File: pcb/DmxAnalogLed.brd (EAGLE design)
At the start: 69 parts, among them IC2 7805TV, J1 RS485, J2 POWER_JACKPTH, J3 RS485, Q1 16MHz 10ppm, U1 ARDUINO_LEONARDO-REV3B_SMARTP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, U2 SN75176ASOIC, X1 USBPTH

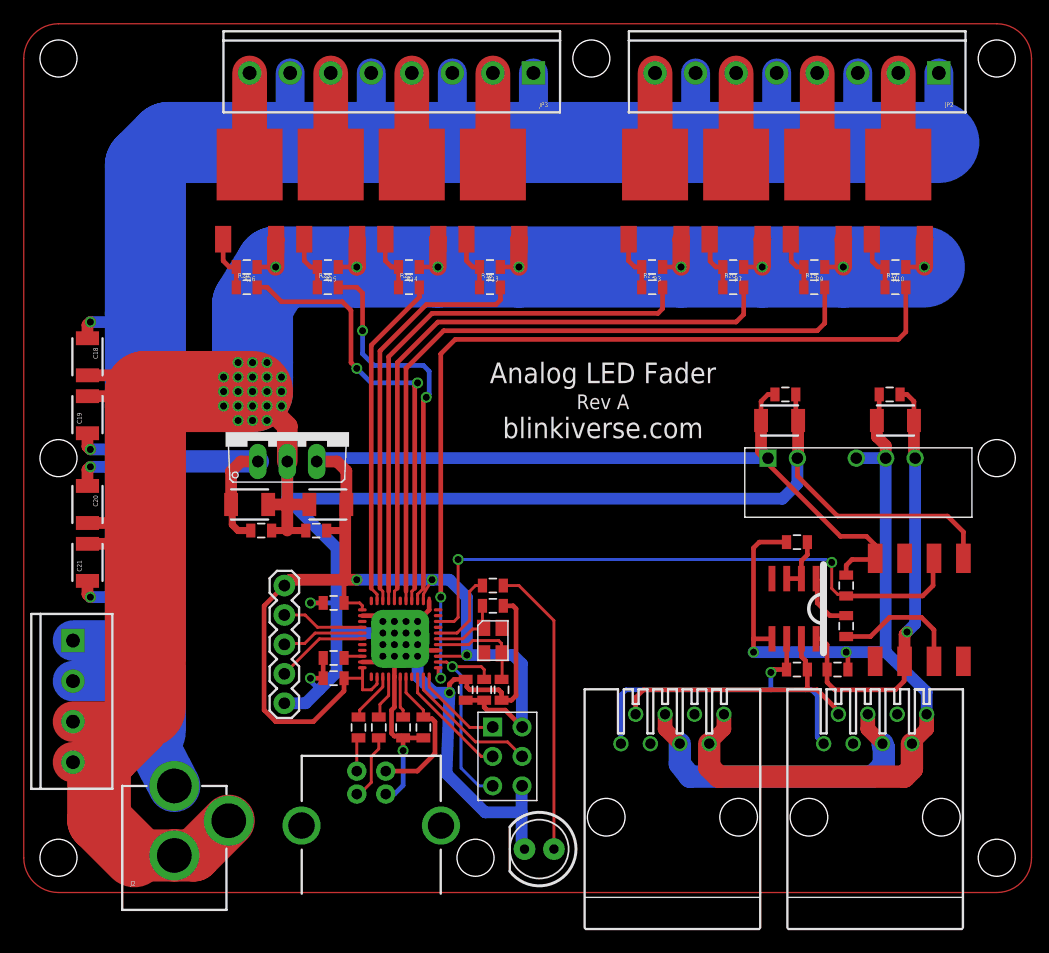
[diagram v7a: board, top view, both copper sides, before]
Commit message: Add extra drain vias, space for mounting holes, line up connectors, drop series gate resistors, fix RX line
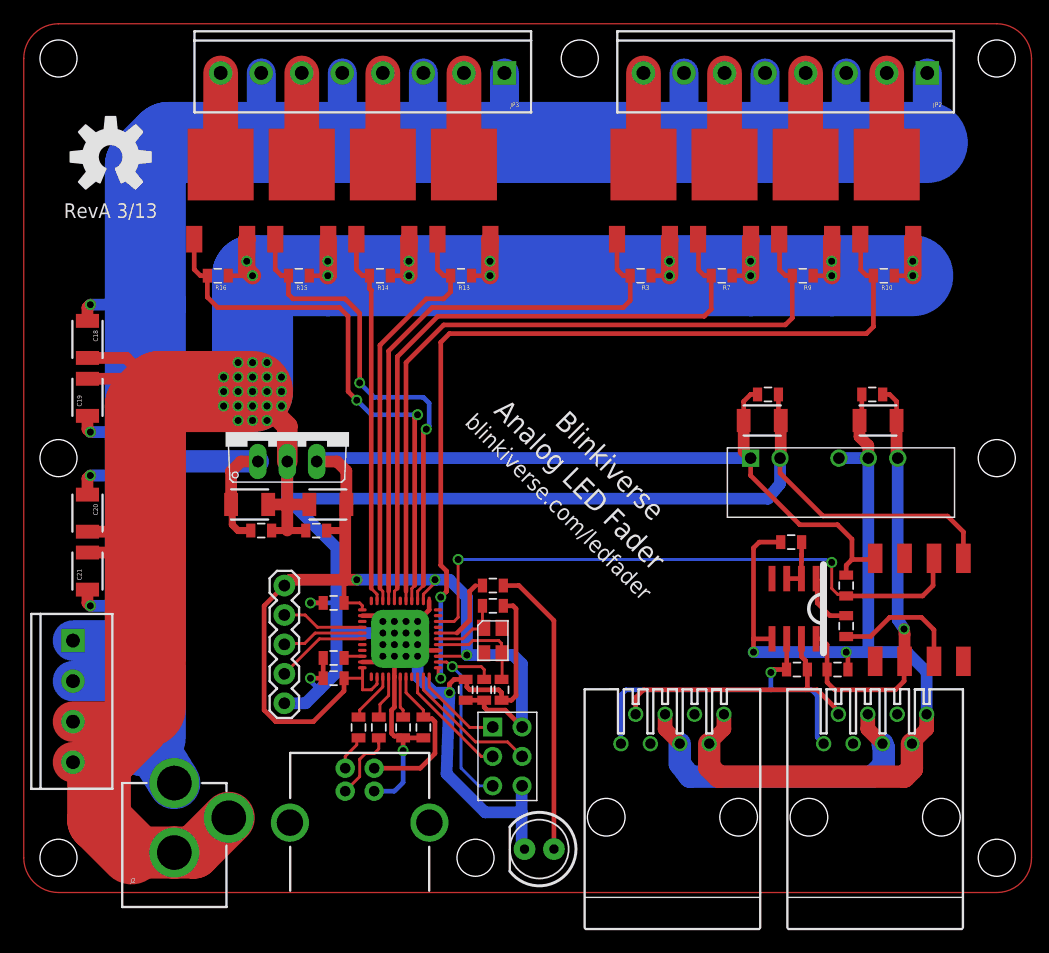
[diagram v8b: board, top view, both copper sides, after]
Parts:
- removed R17, R18, R19, R20, R21, R22, R23, R24: 50, SparkFun:0805
- added U$11: (no value), SparkFun:OSHW-LOGO-L
- moved R13 2.61 mm to (37.8, 53.2)
- moved R14 2.61 mm to (30.8, 53.2)
- moved R15 2.61 mm to (23.8, 53.2)
- moved R16 2.61 mm to (16.8, 53.2)
- moved JP3 2.50 mm to (41.5, 70.8)
- moved U$6 2.50 mm to (38.0, 59.8)
- moved U$7 2.50 mm to (31.0, 59.8)
- moved U$8 2.50 mm to (24.0, 59.8)
- moved U$9 2.50 mm to (17.0, 59.8)
- moved C10 1.50 mm to (73.2, 43.0)
- moved C16 1.50 mm to (63.8, 40.8)
- moved C17 1.50 mm to (73.8, 40.8)
- moved C18 1.50 mm to (5.50, 47.8)
- moved C19 1.50 mm to (5.50, 42.8)
- moved C9 1.50 mm to (64.2, 43.0)
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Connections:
- removed net PWM0_MID: R10.2, R17.1, U$1.P$1
- removed net PWM1_MID: R19.1, R9.2, U$3.P$1
- removed net PWM2_MID: R20.1, R7.2, U$4.P$1
- removed net PWM3_MID: R21.1, R3.2, U$5.P$1
- removed net PWM4_MID: R13.2, R18.1, U$6.P$1
- removed net PWM5_MID: R14.2, R22.1, U$7.P$1
- removed net PWM6_MID: R15.2, R23.1, U$8.P$1
- removed net PWM7_MID: R16.2, R24.1, U$9.P$1
- net PWM0: now also R10.2, U$1.P$1; no longer R17.2
- net PWM1: now also R9.2, U$3.P$1; no longer R19.2
- net PWM2: now also R7.2, U$4.P$1; no longer R20.2
- net PWM3: now also R3.2, U$5.P$1; no longer R21.2
- net PWM4: now also R13.2, U$6.P$1; no longer R18.2
- net PWM5: now also R14.2, U$7.P$1; no longer R22.2
- net PWM6: now also R15.2, U$8.P$1; no longer R23.2
- net PWM7: now also R16.2, U$9.P$1; no longer R24.2
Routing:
- net PWM7: track 38.9 -> 48.3 mm
- net GND: track 405.4 -> 414.1 mm
- net PWM6: track 34.2 -> 42.6 mm
- net PWM7_MID: track 4.97 -> 0.00 mm
- net PWM6_MID: track 4.97 -> 0.00 mm
- net PWM5_MID: track 4.97 -> 0.00 mm
- net PWM4_MID: track 4.97 -> 0.00 mm
- net PWM3_MID: track 4.97 -> 0.00 mm
- net PWM2_MID: track 4.97 -> 0.00 mm
- net PWM1_MID: track 4.97 -> 0.00 mm
- net PWM0_MID: track 4.97 -> 0.00 mm
- net PWM5: track 29.0 -> 32.3 mm
- net PWM0: track 73.8 -> 76.7 mm
- net PWM2: track 54.6 -> 56.8 mm
- net PWM1: track 60.9 -> 63.1 mm
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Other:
- board text added: "Blinkiverse"
- board text added: "RevA 3/13"
- board text added: "blinkiverse.com/ledfader"
- board text removed: "Rev A"
- board text removed: "blinkiverse.com"
